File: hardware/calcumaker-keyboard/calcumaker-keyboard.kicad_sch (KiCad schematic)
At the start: 0 parts

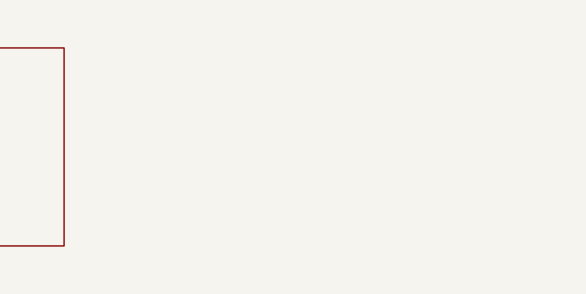
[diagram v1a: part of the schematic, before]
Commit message: hardware: per-key RGB hint lighting on the keyboard board (50x SK6805 on gated VSYS) (#4)
Add addressable RGB accent lighting that hints key positions / presses -- one
SK6805-EC15 (1.5x1.5mm, the smallest serial RGB with a KiCad footprint + real
LCSC stock, C2890035) beside each of the 50 keys, single-wire daisy chain off
one STM32G0 pin.

Power: the LEDs are ~5V parts and the keyboard rail is only 3.3V, so they run
off VSYS (the MCU board's load-shared battery/USB rail, ~3.7-4.7V) brought up a
WIDENED 12-pin mezzanine (10 -> 12: +VSYS +GND). A high-side P-FET load switch
(Q1 AO3401A + Q2 2N7002) gates the whole LED rail off in sleep (G0 LED_EN) to
protect battery life, and a 74LVC1G125 (powered from the gated rail) level-shifts
the 3.3V data up to the LED VIH.

- calcumaker-keyboard: new KeyLighting sheet (50x SK6805 D56-D105 + U2 shifter +
  Q1/Q2 load switch + R7-R10 / C6-C7); J1 mezzanine -> 12-pin DF40C-12DP
  (C6224952). 119 -> 178 components.
- calcumaker-mcu: J5 mezzanine -> 12-pin DF40B-12DS (C3641147); route VSYS.
- DF40 stack: the receptacle SUFFIX sets the mated height (none = 1.5mm,
  (2.0) = 2.0mm, H-series = 2.5-4.0mm), NOT the B/C letter; the DF40C plug is the
  common header -- so DF40C-12DP x DF40B-12DS is a valid 1.5mm stack, same as the
  original 10-pin (DF40C-12DS just isn't LCSC-stocked).
- DESIGN.md / PARTS.md / memory: RGB subsystem, 12-pin pinout, BOM rows, the
  sleep-gate + current-cap notes (firmware must cap total brightness; 50x
  full-white ~0.75A would exceed the DF40 / VSYS budget).

All three boards regenerate + pass the structure check (mcu 55 / keyboard 178 /
display 60, no duplicate refs).

Co-authored-by: Claude Opus 4.8 (1M context) <noreply@anthropic.com>
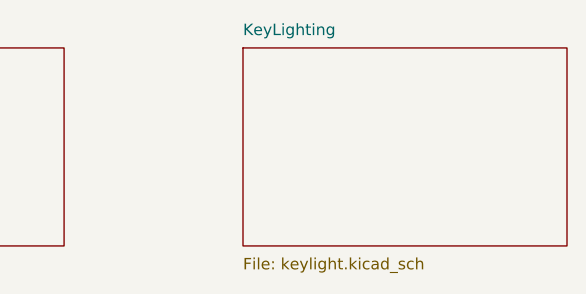
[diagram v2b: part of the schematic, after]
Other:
- added sheet KeyLighting (keylight.kicad_sch)
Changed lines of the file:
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@@
 	(title_block
 		(title "Calcumaker 16 — Keyboard")
-		(date "2026-07-05")
-		(rev "0.2")
+		(date "2026-07-06")
+		(rev "0.3")
 		(company "calcumaker authors")
 		(comment 1 "Programmer's/technical arbitrary-precision RPN calculator")
-		(comment 2 "Keyboard board: Cherry MX matrix + STM32G0 scanner + annunciators + MCU mezzanine (DRAFT)")
+		(comment 2 "Keyboard board: Cherry MX matrix + STM32G0 scanner + annunciators + per-key RGB (gated) + MCU mezzanine (DRAFT)")
 	)
 	(sheet
@@
 			(effects (font (size 1.27 1.27)) (justify left top))
 		)
+	)
+	(sheet
+		(at 264.16 40.64)
+		(size 36.00 22.00)
+		(fields_autoplaced yes)
+		(stroke (width 0.1524) (type solid))
+		(fill (color 0 0 0 0.0000))
+		(property "Sheetname" "KeyLighting"
+			(at 264.16 39.37 0)
+			(effects (font (size 1.27 1.27)) (justify left bottom))
+		)
+		(property "Sheetfile" "keylight.kicad_sch"
+			(at 264.16 63.91 0)
+			(effects (font (size 1.27 1.27)) (justify left top))
+		)

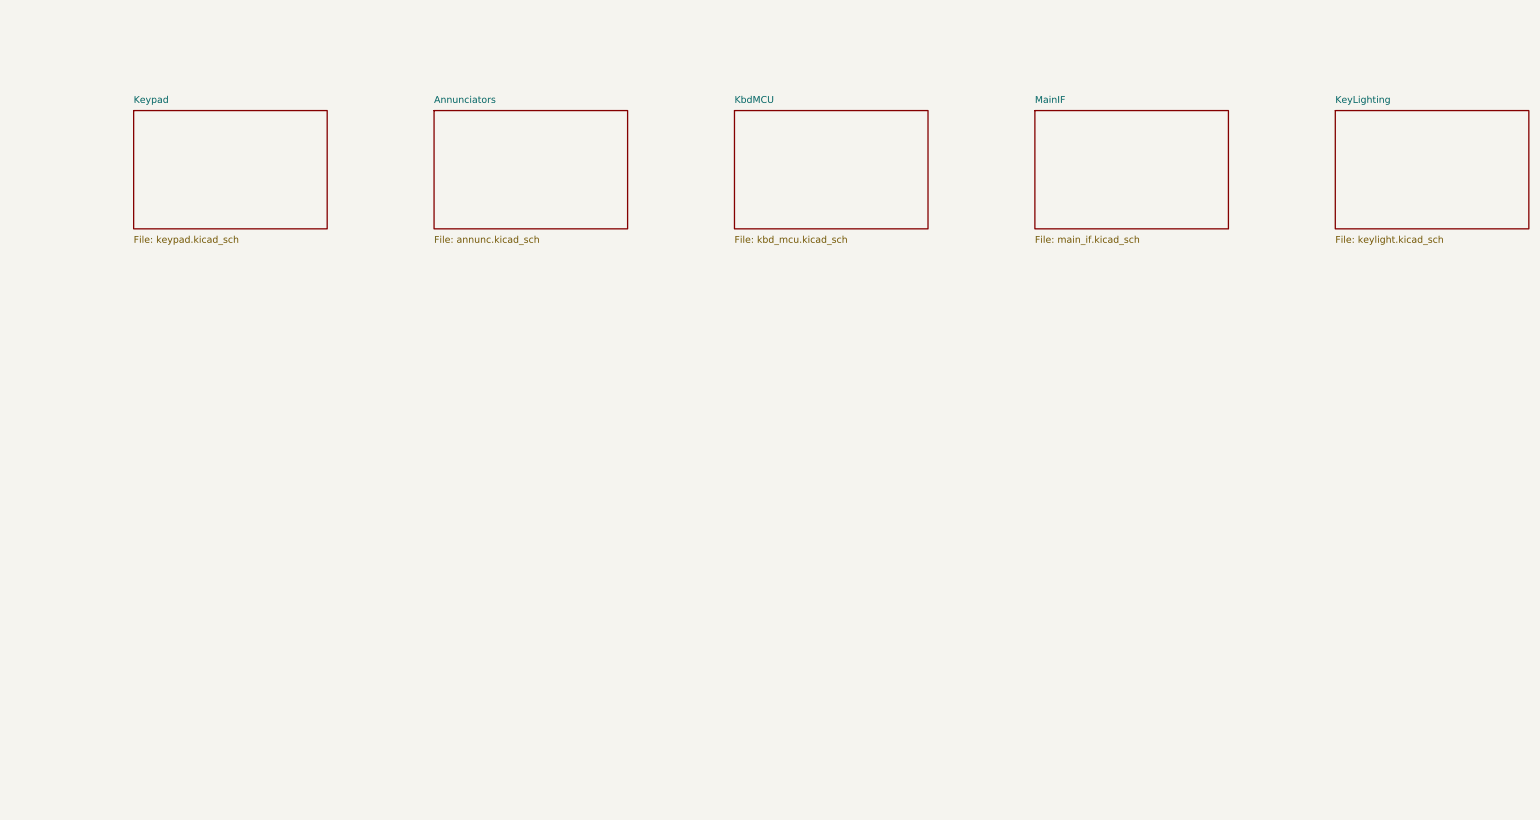
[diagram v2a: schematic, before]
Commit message: hardware: keyboard as a multi-channel design (reusable 10-key row x5) (#5)
Refactor calcumaker-keyboard from a FLAT layout (100 individually-placed SW/D
parts on one sheet + 50 flat RGB LEDs) into a KiCad multi-channel design,
matching the display board.

- key_row.kicad_sch: a reusable 10-key row, FULLY WIRED, instantiated x5
  (Row1-5). Each key = MX switch + 1N4148W diode + SK6805 RGB.
    matrix  SW.1 -> ROW (hier); SW.2 -> KNk -> diode.A; diode.K -> COLk (global)
    RGB     DIN -> LED1..LED10 -> DOUT (hier, chained @root); VDD->VLED, VSS->GND
  Per-instance refs SW1-50 / D1-50 (matrix) / D56-105 (RGB). Shared buses
  (COL1-10, VLED, GND) are global nets; ROW + RGB DIN/DOUT are hierarchical pins
  wired at the root (KB_ROW1-5; KB_LED_DATA -> Row1 -> ... -> Row5 -> RGB_END).
- Split the old KeyLighting sheet -> key_row (the 50 LEDs) + rgb_power (the
  level shifter + gated load switch).
- Converted the whole keyboard manifest from the flat K.build() path to the
  display-style write_wired_child/write_root API; the one-off sheets
  (annunc/kbd_mcu/rgb_power/main_if) stay single-instance, placed via a grid
  helper. Removed the obsolete keypad.kicad_sch + keylight.kicad_sch.
- Docs (DESIGN.md sheet plan, CLAUDE/AGENTS, scripts README) + a few stale fixes
  (STM32U575RGTx, "three boards", current sheet names).

178 components, no duplicate refs, all three boards pass the structure check.
(The 2 lib_symbol_mismatch ERC warnings on the G0/TagConnect are pre-existing
kschgen symbol-cache fidelity, not from this change.)

Co-authored-by: Claude Opus 4.8 (1M context) <noreply@anthropic.com>
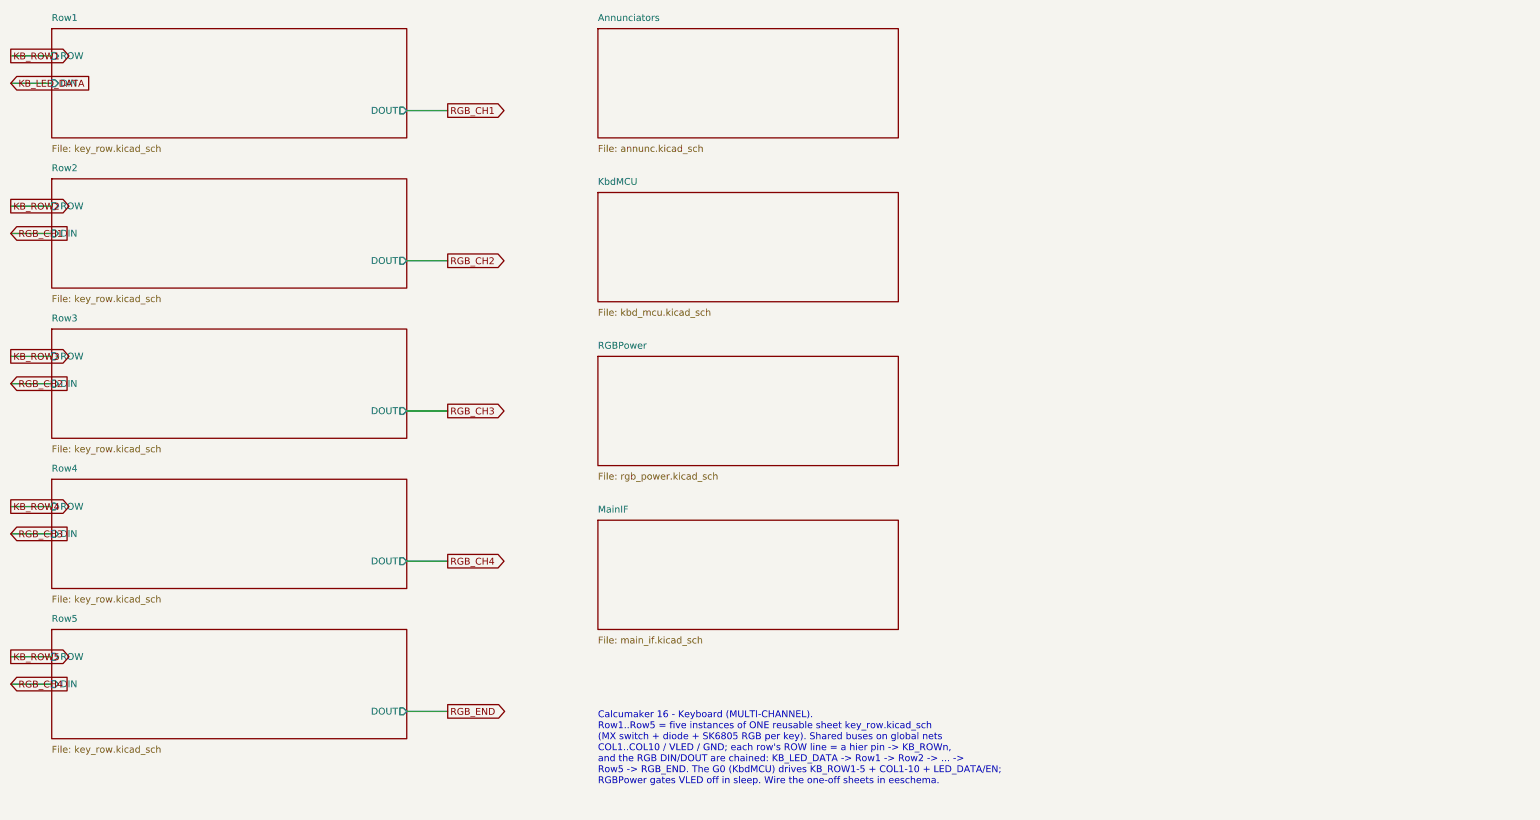
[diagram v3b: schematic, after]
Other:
- removed sheet KeyLighting
- removed sheet Keypad
- added sheet RGBPower (rgb_power.kicad_sch)
- added sheet Row1 (key_row.kicad_sch)
- added sheet Row2 (key_row.kicad_sch)
- added sheet Row3 (key_row.kicad_sch)
- added sheet Row4 (key_row.kicad_sch)
- added sheet Row5 (key_row.kicad_sch)
- note added: "Calcumaker 16 - Keyboard (MULTI-CHANNEL). Row1..Row5 = five instances of ONE reusable sheet key_row.kicad_sch (MX switch + diode + SK6805 RGB per key). Shared buses on global nets COL1..COL10 / VLED / GND; each row's ROW line = a hier pin -> KB_ROWn, and the RGB DIN/DOUT are chained: KB_LED_DATA -> Row1 -> Row2 -> ... -> Row5 -> RGB_END. The G0 (KbdMCU) drives KB_ROW1-5 + COL1-10 + LED_DATA/EN; R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"

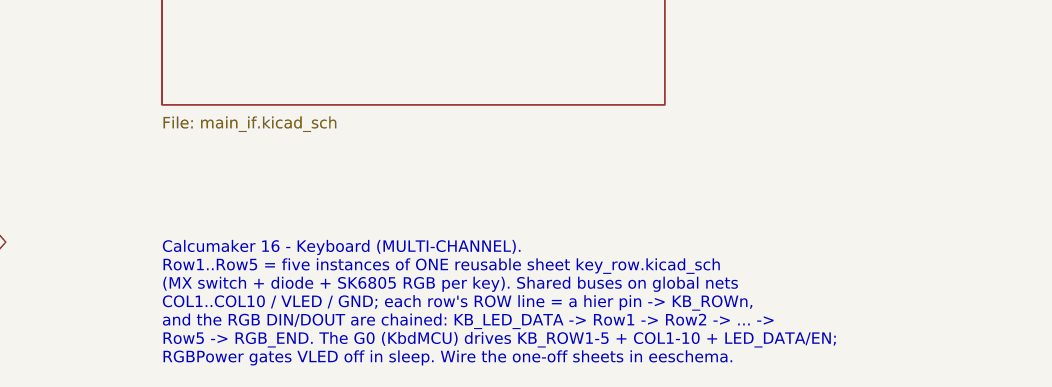
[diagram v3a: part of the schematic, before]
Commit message: hardware: keyswitch 3D models, hot-swap footprint, reverse-mount per-key RGB
Physical build-out of the keyboard: real switch 3D, a hot-swap footprint, and a
single-sided-assembly LED choice.

- 3D models (vendored, hardware/lib/3dmodels): SW_Cherry_MX_1.00u_PCB.step from
  kiswitch/kiswitch (MIT) -- KiCad's Button_Switch_Keyboard.3dshapes does not
  exist in packages3D upstream, so there's nothing to install/download from
  KiCad -- plus HS_CPG151101S11_MX.step (socket) from marbastlib (CERN-OHL-P).
  Also vendor a plain solder-in SW_Cherry_MX_1.00u_PCB.kicad_mod (fallback).

- Keyswitch footprint -> marbastlib SW_MX_HS_CPG151101S11_1u (CERN-OHL-P): the
  Kailh CPG151101S11 hot-swap socket (LCSC C41430893). PLACE-ON-BACK -- switch
  fps go on the board's back copper layer so the socket (authored on F.Cu) lands
  on the physical bottom. HOT-SWAP ONLY: the switch thru-holes are 0.15mm-ring
  socket pass-throughs, NOT solder pads, so a switch-only/solder-in build would
  be a separate board rev (using the vendored solder-in-only fp). The switch-body
  (model) is on the footprint's B side so it renders opposite the socket for
  place-on-back. (Corrects an earlier, wrong "one-board solder+hotswap combo"
  framing -- the pass-throughs don't make a reliable solder joint.)

- Per-key RGB SK6805-EC15 -> SK6812MINI-E (LCSC C5149201), reverse/bottom mount
  (KiCad LED_SK6812MINI-E_3.2x2.8mm_P1.5mm_ReverseMount fp + bundled 3D): the LED
  sits on the bottom with the sockets -> SINGLE-SIDED assembly (one stencil, no
  flip), shining up through the switch's north LED window. Uses the base
  LED:SK6812 symbol (MINI-E `extends` it; kschgen doesn't resolve extends) with
  value/fp/lcsc overridden.

- Docs: DESIGN.md ("Hot-swap switches (place-on-back)" + reverse-mount RGB),
  PARTS.md, both hardware/lib READMEs (with license attribution), memory.

All three boards regenerate + pass the structure check (mcu 55 / keyboard 178 /
display 60, no duplicate refs).

Co-Authored-By: Claude O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
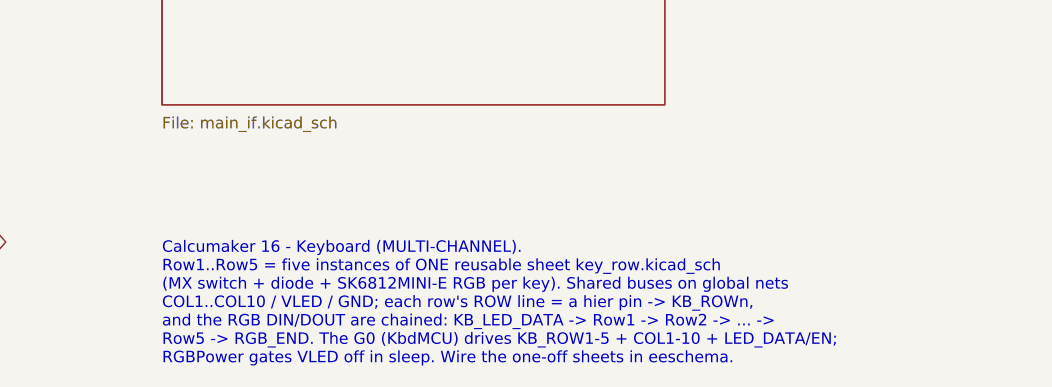
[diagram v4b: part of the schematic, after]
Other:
- note added: "Calcumaker 16 - Keyboard (MULTI-CHANNEL). Row1..Row5 = five instances of ONE reusable sheet key_row.kicad_sch (MX switch + diode + SK6812MINI-E RGB per key). Shared buses on global nets COL1..COL10 / VLED / GND; each row's ROW line = a hier pin -> KB_ROWn, and the RGB DIN/DOUT are chained: KB_LED_DATA -> Row1 -> Row2 -> ... -> Row5 -> RGB_END. The G0 (KbdMCU) drives KB_ROW1-5 + COL1-10 + LED_DATA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"
- note removed: "Calcumaker 16 - Keyboard (MULTI-CHANNEL). Row1..Row5 = five instances of ONE reusable sheet key_row.kicad_sch (MX switch + diode + SK6805 RGB per key). Shared buses on global nets COL1..COL10 / VLED / GND; each row's ROW line = a hier pin -> KB_ROWn, and the RGB DIN/DOUT are chained: KB_LED_DATA -> Row1 -> Row2 -> ... -> Row5 -> RGB_END. The G0 (KbdMCU) drives KB_ROW1-5 + COL1-10 + LED_DATA/EN; R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"
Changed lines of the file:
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@@
 		(effects (font (size 1.27 1.27)) (justify left))
 	)
-	(text "Calcumaker 16 - Keyboard (MULTI-CHANNEL).\nRow1..Row5 = five instances of ONE reusable sheet key_row.kicad_sch\n(MX switch + diode + SK6805 RGB per key). Shared buses on global nets\nCOL1..COL10 / VLED / GND; each row's ROW line = a hier pin -> KB_ROWn,\nand the RGB DIN/DOUT are chained: KB_LED_DATA -> Row1 -> Row2 -> ... ->\nRow5 -> RGB_END. The G0 (KbdMCU) drives KB_ROW1-5 + COL1-10 + LED_DATA/EN;\nRGBPower gates VLED off in sleep. Wire the one-off sheets in eeschema."
+	(text "Calcumaker 16 - Keyboard (MULTI-CHANNEL).\nRow1..Row5 = five instances of ONE reusable sheet key_row.kicad_sch\n(MX switch + diode + SK6812MINI-E RGB per key). Shared buses on global nets\nCOL1..COL10 / VLED / GND; each row's ROW line = a hier pin -> KB_ROWn,\nand the RGB DIN/DOUT are chained: KB_LED_DATA -> Row1 -> Row2 -> ... ->\nRow5 -> RGB_END. The G0 (KbdMCU) drives KB_ROW1-5 + COL1-10 + LED_DATA/EN;\nRGBPower gates VLED off in sleep. Wire the one-off sheets in eeschema."
 		(exclude_from_sim no)
 		(at 127.00 152.40 0)

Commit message: hw: regenerate keyboard for the 2U ENTER + vendor the 2U hot-swap footprint
Board files now reflect the 2U ENTER (49 keys):
- key_row.kicad_sch      -> 4 instances (Row1/2/3/5), 30 symbols
- key_row_9.kicad_sch    -> NEW, 1 instance (Row4), 27 symbols: no switch, diode
                            or RGB LED at COL6; refs keep a hole (no SW36/D36/D91)
- root note + rgb_power note updated (49 LEDs, Row4 has 9)

check-calcumaker-keyboard: 176 components (3 fewer), 176/176 footprints assigned,
no duplicate refs, structure sound. Regeneration verified safe first by running the
generator against a scratch copy: the one-off sheets (annunc/kbd_mcu/main_if)
rebuild byte-identical modulo uuids, i.e. nothing was hand-wired.

Vendored calcumaker:SW_MX_HS_CPG151101S11_2u_Vertical -- the 1u hot-swap footprint
plus the four PCB-mount 2U stabilizer NPTH holes (y = +/-11.90mm = 23.8mm spacing;
each wing a 3.05mm hole at x=-7.00 and a 4.00mm at x=+8.24), taken from stock
Button_Switch_Keyboard:SW_Cherry_MX_2.00u_Vertical_PCB and re-expressed about our
origin (already the switch centre). Courtyard grown; 2U keycap envelope on F.Fab.
KiCad 10 parses/plots it (kicad-cli fp export svg).

It is UNUSED by default: we use PLATE-mount stabilizers, which clip into the
switch plate the hot-swap sockets already require, so the PCB needs no stab holes
and ENTER just reuses MX_FP (verified: KiCad's SW_Cherry_MX_2.00u_Vertical_Plate
has the same pad/hole set as the 1u plate fp). PCB-mount would additionally force
a Row5 variant sheet, since ENTER's switch is on the shared 10-key sheet.

Place-on-back is safe: mirroring X maps the stab-hole set onto itself rotated 180,
and a 2U key is symmetric.

Co-Authored-By: Claude Opus 4.8 (1M context) <noreply@anthropic.com>
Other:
- sheet Row4: file key_row.kicad_sch -> key_row_9.kicad_sch
- note added: "Calcumaker 16 - Keyboard (MULTI-CHANNEL). Row1/2/3/5 = four instances of the reusable 10-key sheet key_row.kicad_sch. Row4 = key_row_9.kicad_sch: 9 keys, no switch/diode/RGB at COL6 -- that is the upper half of the 2U ENTER cap (switch lives in Row5/COL6). 49 keys. (MX switch + diode + SK6812MINI-E RGB per key). Shared buses on global nets COL1..COL10 / VLED / GND; each row's ROW line = a hier pi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"
- note removed: "Calcumaker 16 - Keyboard (MULTI-CHANNEL). Row1..Row5 = five instances of ONE reusable sheet key_row.kicad_sch (MX switch + diode + SK6812MINI-E RGB per key). Shared buses on global nets COL1..COL10 / VLED / GND; each row's ROW line = a hier pin -> KB_ROWn, and the RGB DIN/DOUT are chained: KB_LED_DATA -> Row1 -> Row2 -> ... -> Row5 -> RGB_END. The G0 (KbdMCU) drives KB_ROW1-5 + COL1-10 + LED_DATA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"
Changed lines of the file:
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@@
 			(effects (font (size 1.27 1.27)) (justify left bottom))
 		)
-		(property "Sheetfile" "key_row.kicad_sch"
+		(property "Sheetfile" "key_row_9.kicad_sch"
 			(at 25.4000 130.8100 0)
 			(effects (font (size 1.27 1.27)) (justify left top))
@@
 		(effects (font (size 1.27 1.27)) (justify left))
 	)
-	(text "Calcumaker 16 - Keyboard (MULTI-CHANNEL).\nRow1..Row5 = five instances of ONE reusable sheet key_row.kicad_sch\n(MX switch + diode + SK6812MINI-E RGB per key). Shared buses on global nets\nCOL1..COL10 / VLED / GND; each row's ROW line = a hier pin -> KB_ROWn,\nand the RGB DIN/DOUT are chained: KB_LED_DATA -> Row1 -> Row2 -> ... ->\nRow5 -> RGB_END. The G0 (KbdMCU) drives KB_ROW1-5 + COL1-10 + LED_DATA/EN;\nRGBPower gates VLED off in sleep. Wire the one-off sheets in eeschema."
+	(text "Calcumaker 16 - Keyboard (MULTI-CHANNEL).\nRow1/2/3/5 = four instances of the reusable 10-key sheet key_row.kicad_sch.\nRow4 = key_row_9.kicad_sch: 9 keys, no switch/diode/RGB at COL6 -- that is\nthe upper half of the 2U ENTER cap (switch lives in Row5/COL6). 49 keys.\n(MX switch + diode + SK6812MINI-E RGB per key). Shared buses on global nets\nCOL1..COL10 / VLED / GND; each row's ROW line = a hier pin -> KB_ROWn,\nand the RGB DIN/DOUT are chained: KB_LED_DATA -> Row1 -> Row2 -> ... ->\nRow5 -> RGB_END. The G0 (KbdMCU) drives KB_ROW1-5 + COL1-10 + LED_DATA/EN;\nRGBPower gates VLED off in sleep. Wire the one-off sheets in eeschema."
 		(exclude_from_sim no)
 		(at 127.00 152.40 0)
